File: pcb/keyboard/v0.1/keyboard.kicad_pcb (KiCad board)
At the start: 4 copper layers, 80 x 51 mm, 113 parts, among them J1 USB2.0, J2 SWD, SW1 SPACE, SW13 TAB, SW14 Q, SW15 W, SW16 E, SW17 R, SW18 T, SW19 Y, SW2 SPACE, SW20 U, SW21 I, SW22 O, SW23 P, SW24 RETURN, SW25 CAPS, SW26 A, SW27 S, SW28 D, SW29 F, SW30 G, SW31 H, SW32 J, SW33 K, SW34 L, SW35 SEMI, SW36 QUOTE, SW37 LSHIFT, SW38 Z, SW39 X, SW40 C, SW41 V, SW42 B, SW43 N, SW44 M, SW45 COMMA, SW46 DOT, SW47 QUEST, SW48 RSHIFT, SW49 FN, SW50 LCTRL, SW51 LSUPER, SW52 LALT, SW54 RALT, SW55 RSUPER, SW56 MENU, SW57 RCTRL, SW59 C2, SW62 C5, U1 MDBT50Q-P1MV2, Y1 32.768

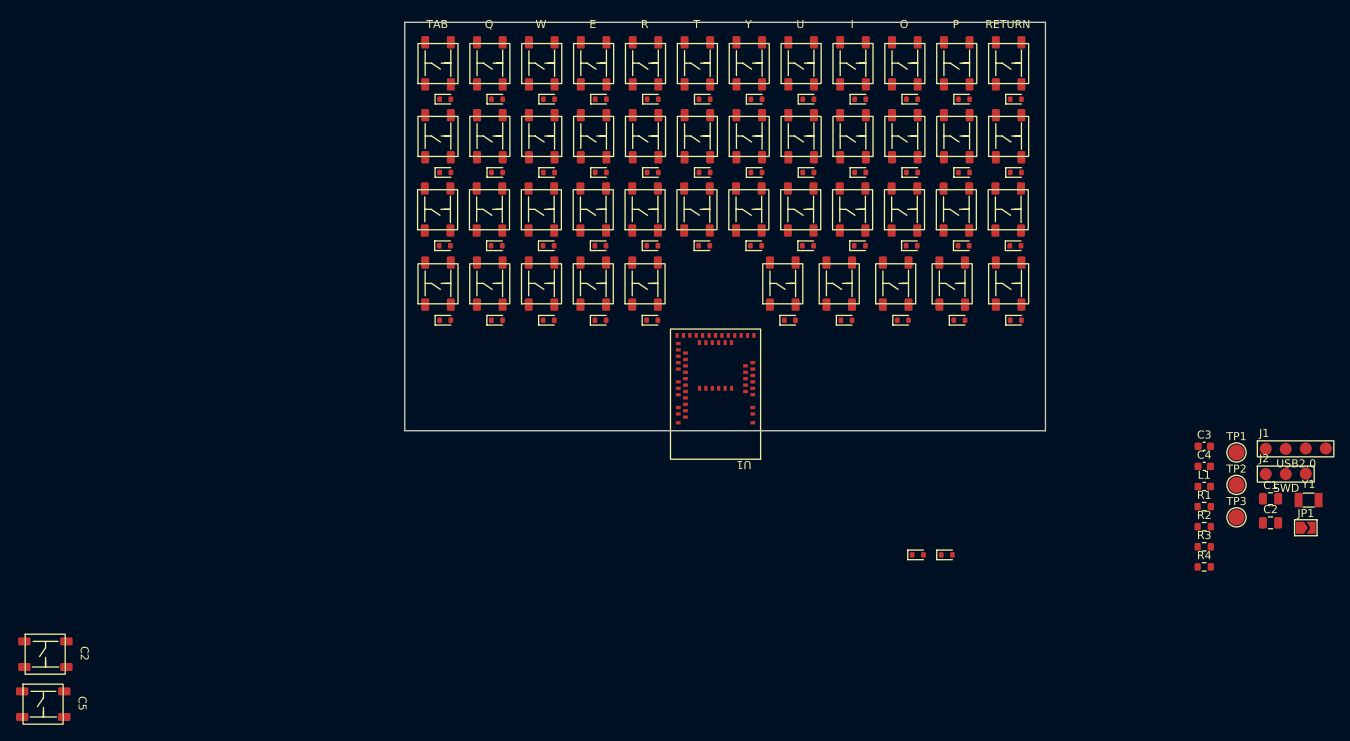
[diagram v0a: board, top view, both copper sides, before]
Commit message: New layout again. Also 7 macro keys now to fill the space
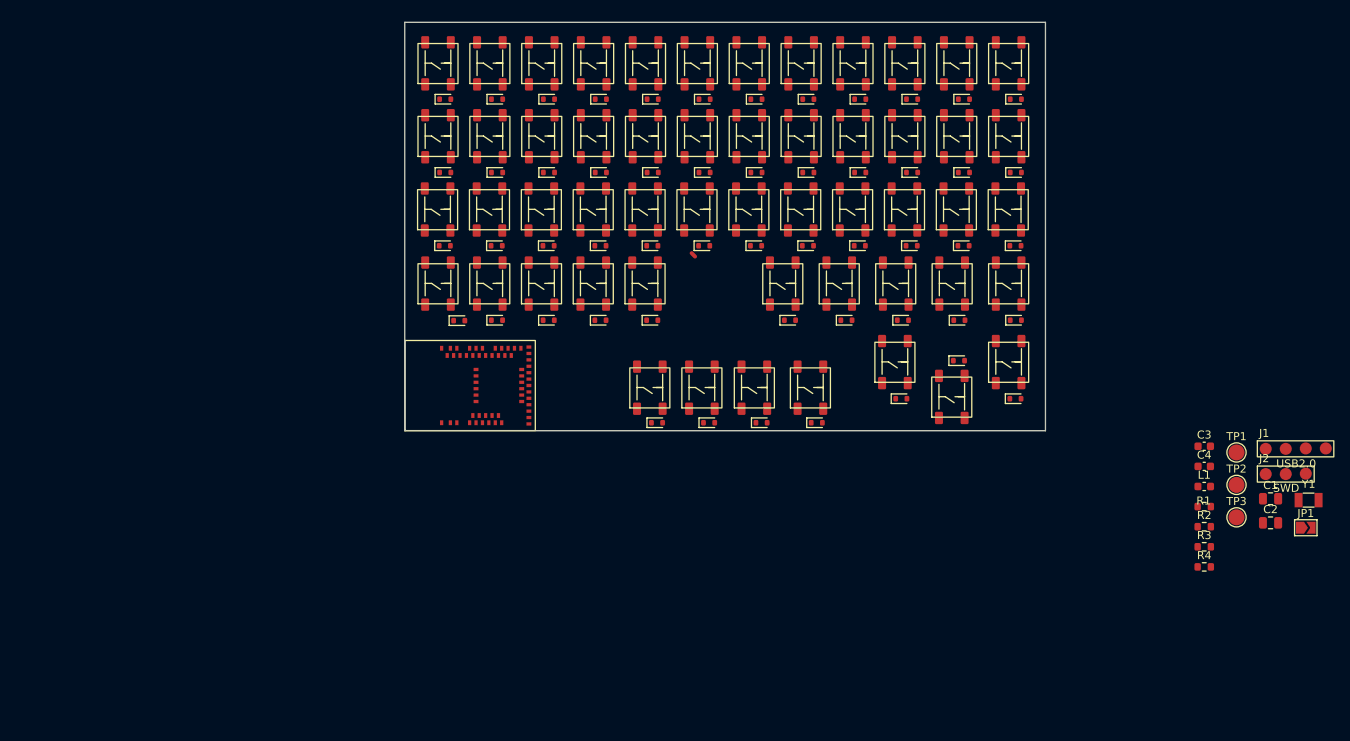
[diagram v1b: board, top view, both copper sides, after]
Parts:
- added D47: 1N4148, Diode_SMD:D_SOD-523, F.Cu at (56.5, 86.0)
- added D49: 1N4148, Diode_SMD:D_SOD-523, F.Cu at (69.5, 86.0)
- added D50: 1N4148, Diode_SMD:D_SOD-523, F.Cu at (76.5, 86.0)
- added D52: 1N4148, Diode_SMD:D_SOD-523, F.Cu at (94.2, 78.2)
- added D53: 1N4148, Diode_SMD:D_SOD-523, F.Cu at (101.2, 83.0)
- added SW47: C1, TH-A1OC:tact_switch_4.5x4.5_PTS647, F.Cu at (54.0, 84.2)
- added SW49: C3, TH-A1OC:tact_switch_4.5x4.5_PTS647, F.Cu at (67.0, 84.2)
- added SW50: C4, TH-A1OC:tact_switch_4.5x4.5_PTS647, F.Cu at (74.0, 84.2)
- added SW52: C6, TH-A1OC:tact_switch_4.5x4.5_PTS647, F.Cu at (91.7, 85.4)
- added SW53: C7, TH-A1OC:tact_switch_4.5x4.5_PTS647, F.Cu at (98.8, 81.0)
- SW45: renamed from SW56; value MENU -> C8
- moved SW51 114.1 mm to (84.6, 81.0), turned to 90 degrees
- moved SW48 87.9 mm to (60.5, 84.2), turned to 90 degrees
- moved U1 44.7 mm to (25.0, 87.1), turned to 90 degrees
- moved D48 30.8 mm to (63.0, 86.0)
- moved D51 20.3 mm to (87.0, 83.0)
- moved D37 1.75 mm to (31.8, 73.2)
- renumbered D13 to D1, D22 to D10, D23 to D11, D24 to D12, D25 to D13, D26 to D14, D27 to D15, D28 to D16, D29 to D17, D30 to D18, D31 to D19, D14 to D2, D32 to D20, D33 to D21, D34 to D22, D35 to D23, D36 to D24, D37 to D25, D38 to D26, D39 to D27, D40 to D28, D41 to D29, D15 to D3, D42 to D30, D43 to D31, D44 to D32, D45 to D33, D46 to D34, D47 to D35, D48 to D36, D49 to D37, D50 to D38, D51 to D39, D16 to D4, D52 to D40, D1 to D41, D2 to D42, D54 to D43, D55 to D44, D56 to D45, D57 to D46, D59 to D48, D17 to D5, D62 to D51, D18 to D6, D19 to D7, D20 to D8, D21 to D9, SW13 to SW1, SW22 to SW10, SW23 to SW11, SW24 to SW12, SW25 to SW13, SW26 to SW14, SW27 to SW15, SW28 to SW16, SW29 to SW17, SW30 to SW18, SW31 to SW19, SW14 to SW2, SW32 to SW20, SW33 to SW21, SW34 to SW22, SW35 to SW23, SW36 to SW24, SW37 to SW25, SW38 to SW26, SW39 to SW27, SW40 to SW28, SW41 to SW29, SW15 to SW3, SW42 to SW30, SW43 to SW31, SW44 to SW32, SW45 to SW33, SW46 to SW34, SW47 to SW35, SW48 to SW36, SW49 to SW37, SW50 to SW38, SW51 to SW39, SW16 to SW4, SW52 to SW40, SW1 to SW41, SW2 to SW42, SW54 to SW43, SW55 to SW44, SW57 to SW46, SW59 to SW48, SW17 to SW5, SW62 to SW51, SW18 to SW6, SW19 to SW7, SW20 to SW8, SW21 to SW9
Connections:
- D48 pad 1: /INPUT3 -> /INPUT7
- D51 pad 1: /INPUT9 -> /INPUT10
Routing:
- net /SOURCE4: track 0.00 -> 0.60 mm
